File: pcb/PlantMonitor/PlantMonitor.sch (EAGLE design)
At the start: 28 parts, among them IC1 453-00005

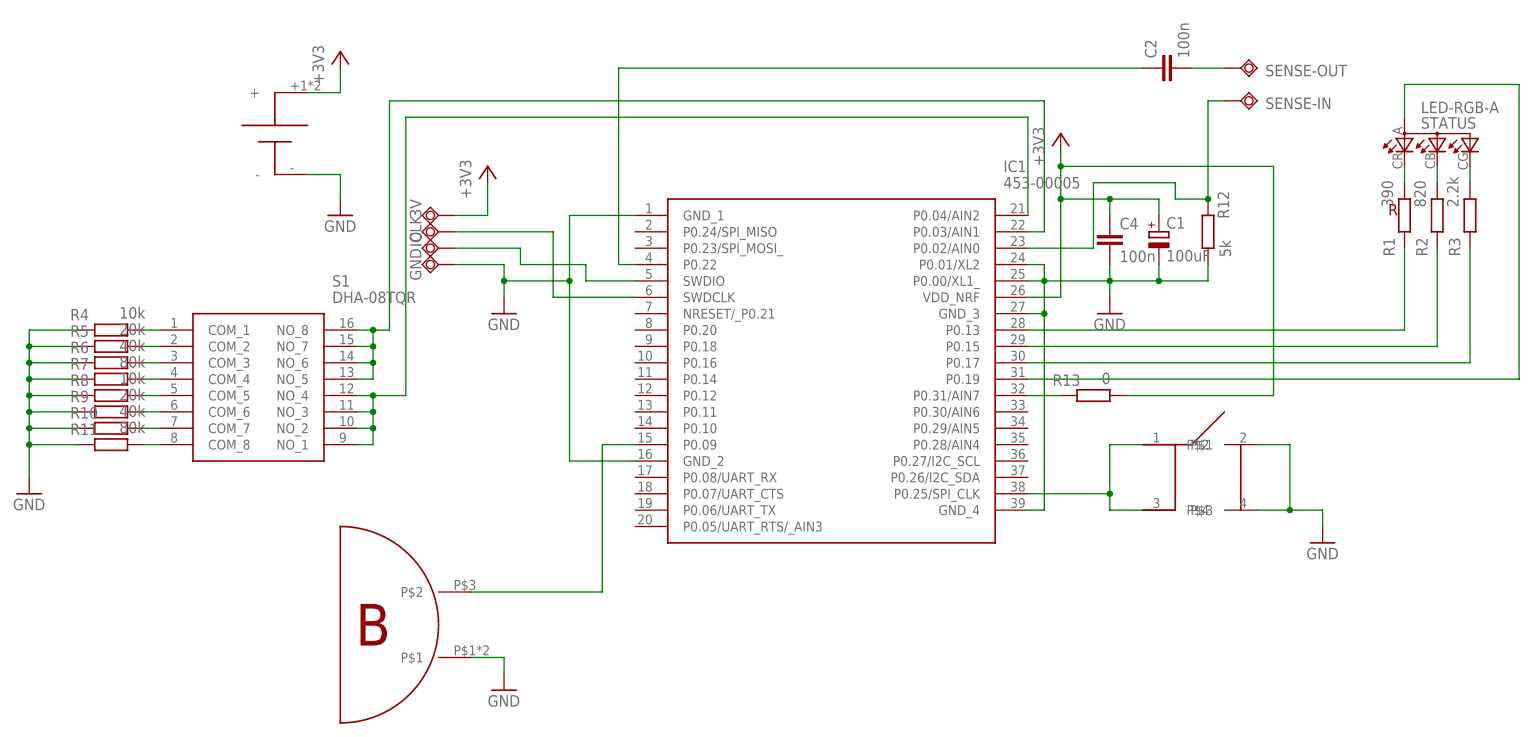
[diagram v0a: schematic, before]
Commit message: Code adoptation for new board - low battery detection - reading ID and sensitivity keys using 2 analogue inputs - improved status indication
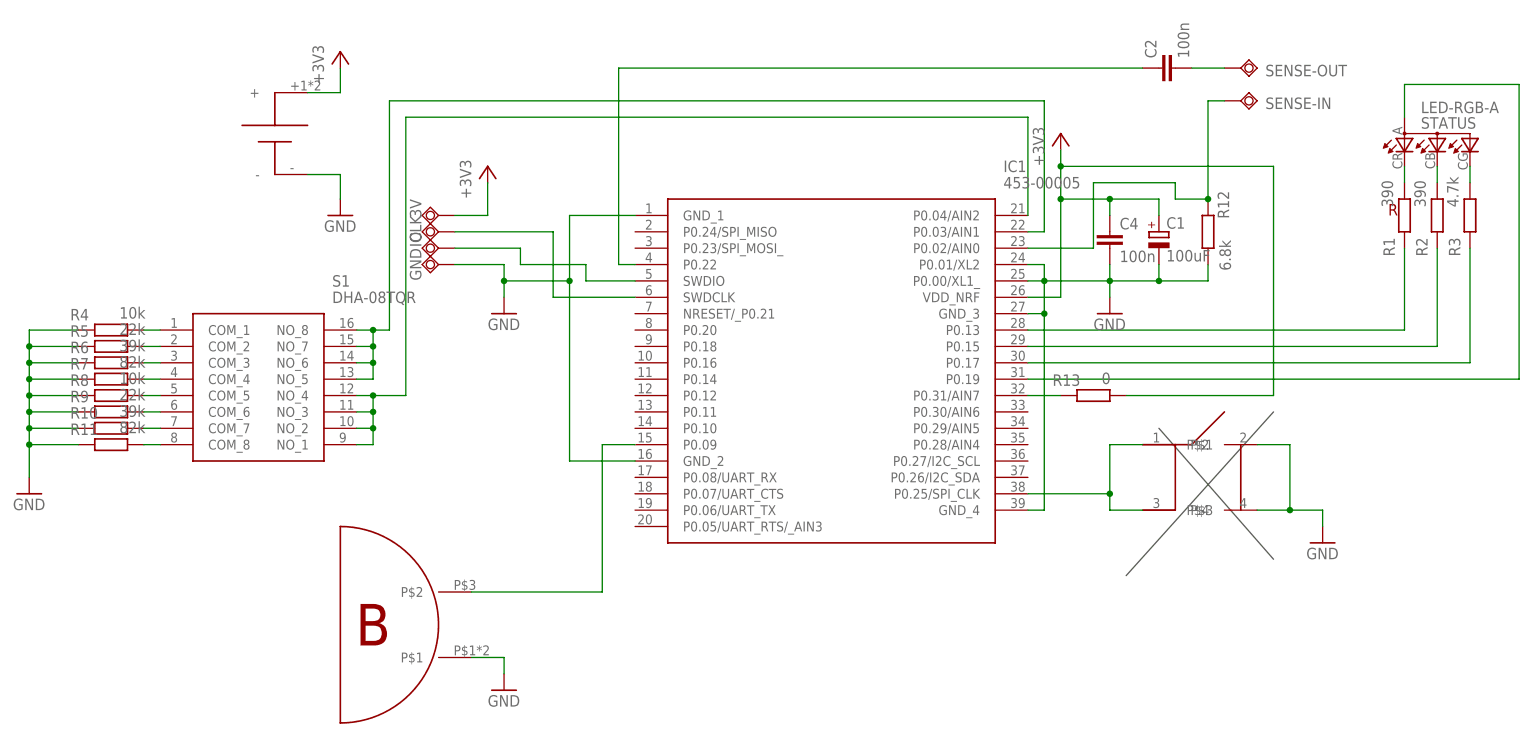
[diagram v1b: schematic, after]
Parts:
- R10, R6: value 40k -> 39k
- R11, R7: value 80k -> 82k
- R12: value 5k -> 6.8k
- R2: value 820 -> 390
- R3: value 2.2k -> 4.7k
- R5, R9: value 20k -> 22k
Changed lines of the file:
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@@
 <parts>
 <part name="IC1" library="SamacSys_Parts" deviceset="453-00005" device=""/>
-<part name="R3" library="rcl" library_urn="urn:adsk.eagle:library:334" deviceset="R-EU_" device="R0603" package3d_urn="urn:adsk.eagle:package:23555/2" value="2.2k"/>
+<part name="R3" library="rcl" library_urn="urn:adsk.eagle:library:334" deviceset="R-EU_" device="R0603" package3d_urn="urn:adsk.eagle:package:23555/2" value="4.7k"/>
 <part name="R1" library="rcl" library_urn="urn:adsk.eagle:library:334" deviceset="R-EU_" device="R0603" package3d_urn="urn:adsk.eagle:package:23555/2" value="390"/>
-<part name="R2" library="rcl" library_urn="urn:adsk.eagle:library:334" deviceset="R-EU_" device="R0603" package3d_urn="urn:adsk.eagle:package:23555/2" value="820"/>
+<part name="R2" library="rcl" library_urn="urn:adsk.eagle:library:334" deviceset="R-EU_" device="R0603" package3d_urn="urn:adsk.eagle:package:23555/2" value="390"/>
 <part name="STATUS" library="STLib" deviceset="LED-RGB-A" device=""/>
 <part name="+3V3" library="supply1" deviceset="+3V3" device="" value="+3V3"/>
@@
 <part name="U$3" library="STLib" deviceset="MICRO-BUZZER" device=""/>
 <part name="GND6" library="supply1" deviceset="GND" device=""/>
-<part name="R12" library="rcl" library_urn="urn:adsk.eagle:library:334" deviceset="R-EU_" device="R0603" package3d_urn="urn:adsk.eagle:package:23555/2" value="5k"/>
+<part name="R12" library="rcl" library_urn="urn:adsk.eagle:library:334" deviceset="R-EU_" device="R0603" package3d_urn="urn:adsk.eagle:package:23555/2" value="6.8k"/>
 <part name="C2" library="rcl" library_urn="urn:adsk.eagle:library:334" deviceset="C-EU" device="C0603K" package3d_urn="urn:adsk.eagle:package:23680/2" value="100n"/>
 <part name="SENSE-OUT" library="testpad" library_urn="urn:adsk.eagle:library:385" deviceset="TPSQ" device="B1,27" package3d_urn="urn:adsk.eagle:package:27944/2"/>
@@
 <part name="GND" library="testpad" library_urn="urn:adsk.eagle:library:385" deviceset="TPSQ" device="B1,27" package3d_urn="urn:adsk.eagle:package:27944/2"/>
 <part name="R4" library="rcl" library_urn="urn:adsk.eagle:library:334" deviceset="R-EU_" device="R0603" package3d_urn="urn:adsk.eagle:package:23555/2" value="10k"/>
-<part name="R5" library="rcl" library_urn="urn:adsk.eagle:library:334" deviceset="R-EU_" device="R0603" package3d_urn="urn:adsk.eagle:package:23555/2" value="20k"/>
-<part name="R6" library="rcl" library_urn="urn:adsk.eagle:library:334" deviceset="R-EU_" device="R0603" package3d_urn="urn:adsk.eagle:package:23555/2" value="40k"/>
-<part name="R7" library="rcl" library_urn="urn:adsk.eagle:library:334" deviceset="R-EU_" device="R0603" package3d_urn="urn:adsk.eagle:package:23555/2" value="80k"/>
+<part name="R5" library="rcl" library_urn="urn:adsk.eagle:library:334" deviceset="R-EU_" device="R0603" package3d_urn="urn:adsk.eagle:package:23555/2" value="22k"/>
+<part name="R6" library="rcl" library_urn="urn:adsk.eagle:library:334" deviceset="R-EU_" device="R0603" package3d_urn="urn:adsk.eagle:package:23555/2" value="39k"/>
+<part name="R7" library="rcl" library_urn="urn:adsk.eagle:library:334" deviceset="R-EU_" device="R0603" package3d_urn="urn:adsk.eagle:package:23555/2" value="82k"/>
 <part name="R8" library="rcl" library_urn="urn:adsk.eagle:library:334" deviceset="R-EU_" device="R0603" package3d_urn="urn:adsk.eagle:package:23555/2" value="10k"/>
-<part name="R9" library="rcl" library_urn="urn:adsk.eagle:library:334" deviceset="R-EU_" device="R0603" package3d_urn="urn:adsk.eagle:package:23555/2" value="20k"/>
-<part name="R10" library="rcl" library_urn="urn:adsk.eagle:library:334" deviceset="R-EU_" device="R0603" package3d_urn="urn:adsk.eagle:package:23555/2" value="40k"/>
-<part name="R11" library="rcl" library_urn="urn:adsk.eagle:library:334" deviceset="R-EU_" device="R0603" package3d_urn="urn:adsk.eagle:package:23555/2" value="80k"/>
+<part name="R9" library="rcl" library_urn="urn:adsk.eagle:library:334" deviceset="R-EU_" device="R0603" package3d_urn="urn:adsk.eagle:package:23555/2" value="22k"/>
+<part name="R10" library="rcl" library_urn="urn:adsk.eagle:library:334" deviceset="R-EU_" device="R0603" package3d_urn="urn:adsk.eagle:package:23555/2" value="39k"/>
+<part name="R11" library="rcl" library_urn="urn:adsk.eagle:library:334" deviceset="R-EU_" device="R0603" package3d_urn="urn:adsk.eagle:package:23555/2" value="82k"/>
 <part name="R13" library="rcl" library_urn="urn:adsk.eagle:library:334" deviceset="R-EU_" device="R0603" package3d_urn="urn:adsk.eagle:package:23555/2" value="0"/>
 </parts>
@@
 <plain>
 <text x="132.08" y="73.66" size="1.778" layer="94">R</text>
+<wire x1="91.44" y1="17.78" x2="114.3" y2="43.18" width="0.1524" layer="97"/>
+<wire x1="96.52" y1="40.64" x2="114.3" y2="20.32" width="0.1524" layer="97"/>
 </plain>
 <instances>
